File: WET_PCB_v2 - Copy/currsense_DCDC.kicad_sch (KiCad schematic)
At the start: 9 parts, among them J17 Capacitor connector, U1 Opamp_Quad

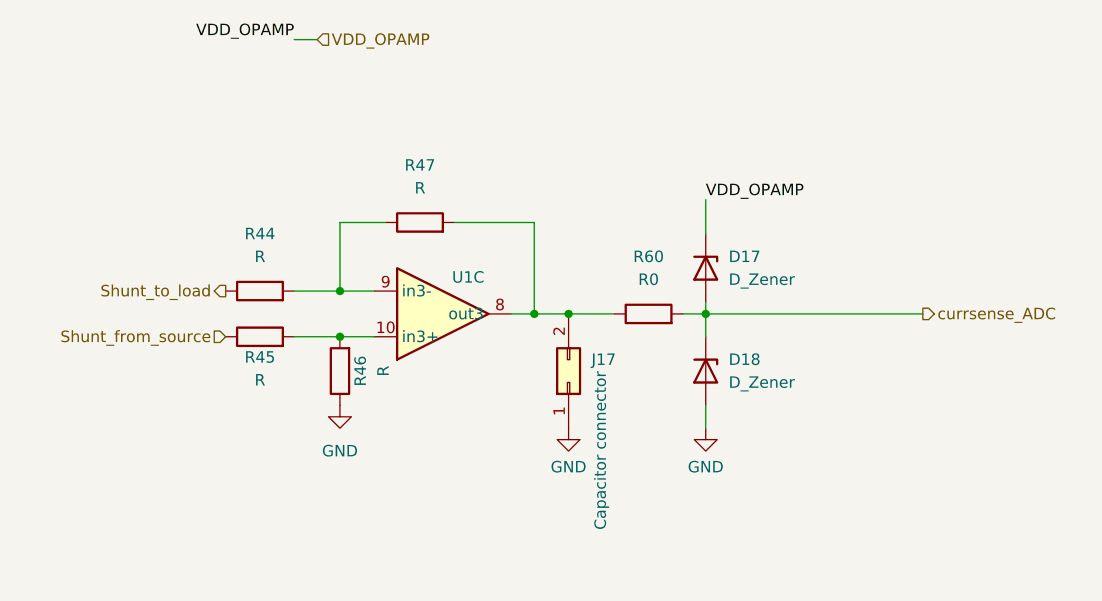
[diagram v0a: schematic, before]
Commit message: microcontroller to chip traces done
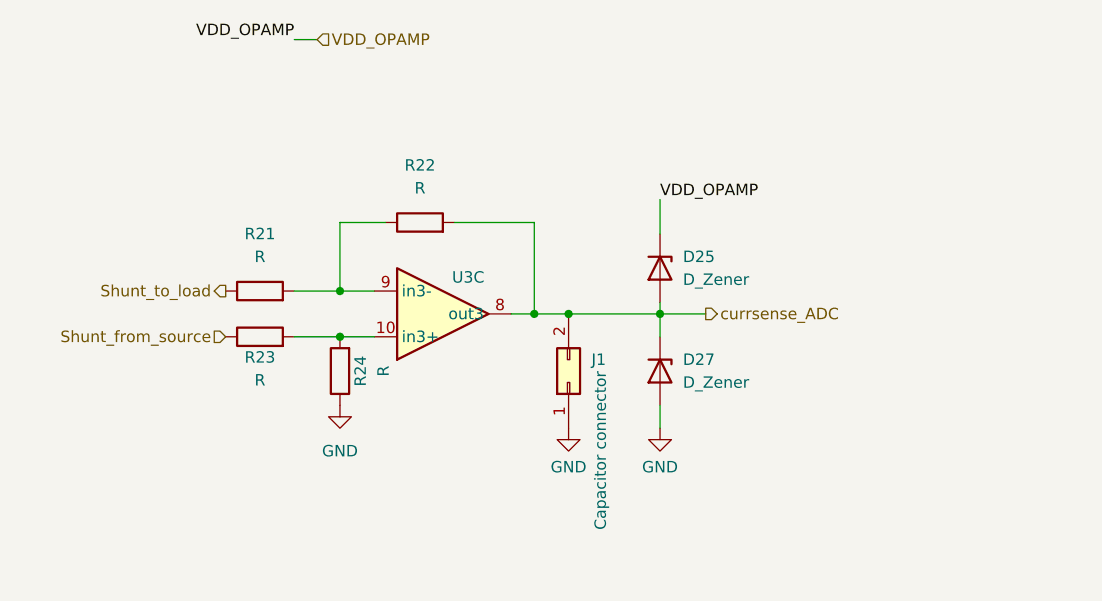
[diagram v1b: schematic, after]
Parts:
- removed R60: R0, Resistor_SMD:R_0805_2012Metric_Pad1.20x1.40mm_HandSolder, symbol Device:R
- D25: renamed from D17; footprint Diode_SMD:D_SMF -> Diode_THT:D_DO-15_P2.54mm_Vertical_CathodeUp
- D27: renamed from D18; footprint Diode_SMD:D_SMF -> Diode_THT:D_DO-15_P2.54mm_Vertical_CathodeUp
- J1: renamed from J17; footprint Connector_PinSocket_2.54mm:PinSocket_1x02_P2.54mm_Horizontal -> Connector_PinSocket_2.54mm:PinSocket_1x02_P2.54mm_Vertical
- renumbered R44 to R21, R47 to R22, R45 to R23, R46 to R24, U1 to U3
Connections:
- net currsense_ADC: now also J1.2 (Pin_2), R22.2, U3.8 (out3)
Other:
- moved on the sheet: D25, D27
